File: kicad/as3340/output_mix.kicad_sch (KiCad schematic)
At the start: 28 parts, among them U1 TL074, U16 LM4040AIM3-2.5, U5 MAX333A, U6 AS3360, U8 DG442CY+

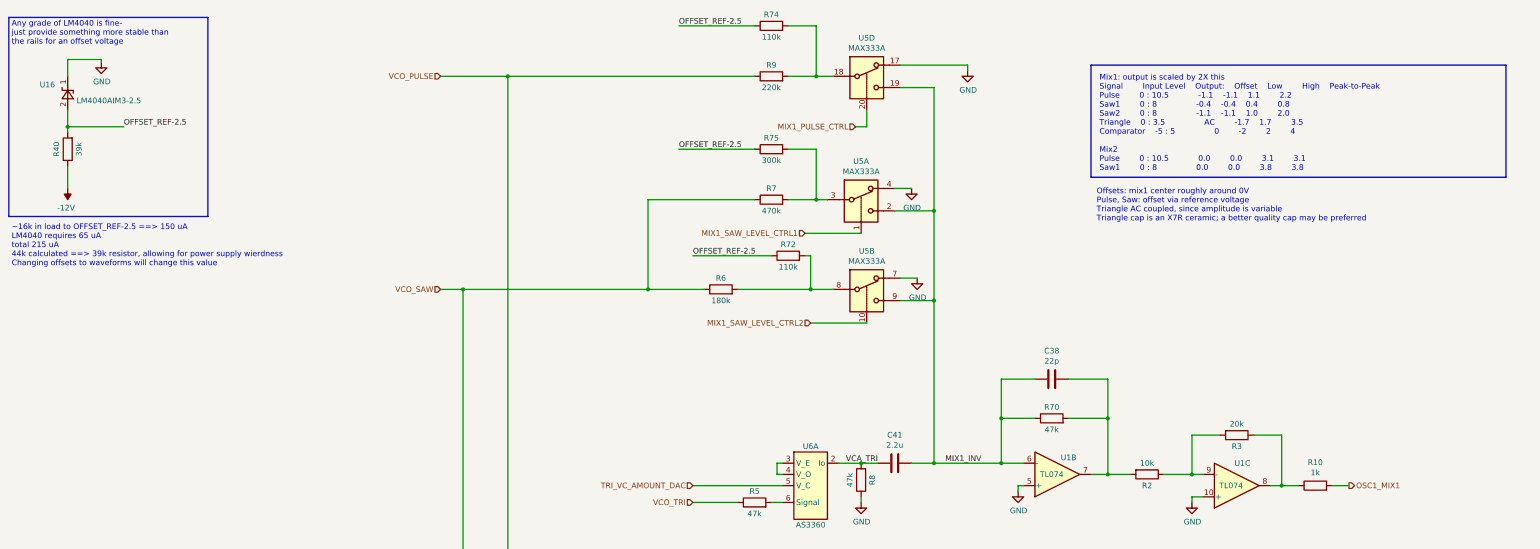
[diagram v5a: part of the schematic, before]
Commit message: working through 3340 changes.  Added sync circuits, DAC scaling changes, 16:1 multiplexor
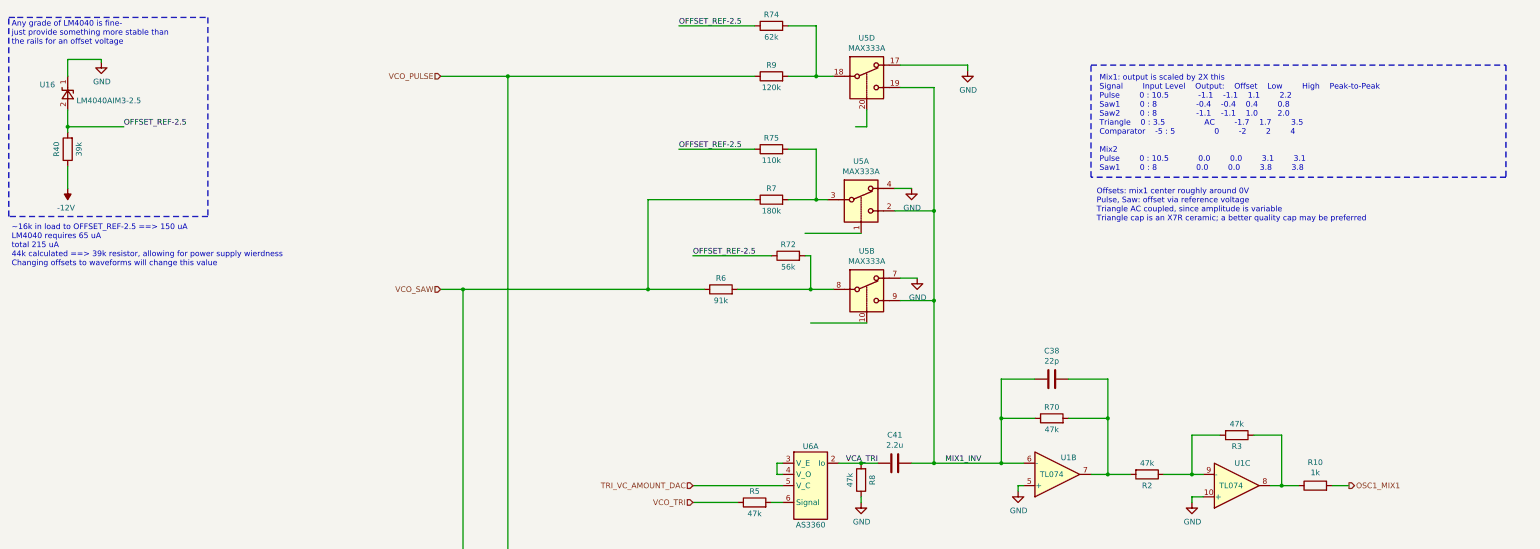
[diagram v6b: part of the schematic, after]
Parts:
- R2: value 10k -> 47k
- R3: value 20k -> 47k
- R6: value 180k -> 91k
- R7: value 470k -> 180k
- R72: value 110k -> 56k
- R74: value 110k -> 62k
- R75: value 300k -> 110k
- R9: value 220k -> 120k
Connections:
- net MIX1_PULSE_CTRL: no longer names the net of U5.20
- net MIX1_SAW_LEVEL_CTRL1: no longer names the net of U5.1
- net MIX1_SAW_LEVEL_CTRL2: no longer names the net of U5.10

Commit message: schematic capture z3340 about done; starting placement
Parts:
- removed R40: 39k, Resistor_SMD:R_0603_1608Metric, symbol Device:R
- removed R72: 56k, Resistor_SMD:R_0603_1608Metric, symbol Device:R
- removed R74: 62k, Resistor_SMD:R_0603_1608Metric, symbol Device:R
- removed R75: 110k, Resistor_SMD:R_0603_1608Metric, symbol Device:R
- removed U16: LM4040AIM3-2.5, Package_TO_SOT_SMD:SOT-23, symbol Reference_Voltage:LM4040DBZ-2.5
- removed U5: MAX333A, Package_SO:SOIC-20W_7.5x12.8mm_P1.27mm, symbol Analog_Switch:MAX333A
- removed U6: AS3360, Package_SO:SOIC-14_3.9x8.7mm_P1.27mm, symbol as3340:AS3360-Audio
- added C51: 2u2, Capacitor_THT:C_Rect_L7.2mm_W5.5mm_P5.00mm_FKS2_FKP2_MKS2_MKP2, symbol Device:C
- added R41: 150k, Resistor_SMD:R_0603_1608Metric, symbol Device:R
- added R43: 12k, Resistor_SMD:R_0603_1608Metric, symbol Device:R
- added U21: AS3364, Package_SO:SOIC-16_3.9x9.9mm_P1.27mm, symbol as3340:AS3364
- added U4: TL072, Package_SO:SSOP-8_3.9x5.05mm_P1.27mm, symbol Amplifier_Operational:TL072
- C41: value 2.2u -> 2u2; footprint Capacitor_SMD:C_1206_3216Metric -> Capacitor_THT:C_Rect_L7.2mm_W5.5mm_P5.00mm_FKS2_FKP2_MKS2_MKP2; LCSC Part C50254 -> (none)
- R7: value 180k -> 47k; LCSC Part (none) -> C25819
- U1: footprint Package_SO:SOIC-14_3.9x8.7mm_P1.27mm -> Package_SO:TSSOP-14_4.4x5mm_P0.65mm; LCSC Part C6963 -> C96507
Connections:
- net GND: now also R41.1, U4.5 (+); no longer R8.1
- net MIX2_PULSE_CTRL: now also U8.8; no longer U8.1
- net MIX2_SAW_CTRL: now also U8.9; no longer U8.16
- net VCO_PULSE: now also U8.7, R41.2; no longer U8.3
- net VCO_SAW: now also U8.11; no longer R7.1, U8.14
- net at R9.2: now also U21.7 (Iin)
- net at R13.1: now also U8.6; no longer U8.2
- net at R14.1: now also U8.10; no longer U8.15
- net at R2.1, R3.2, U1.9 (-): now also R43.2
- net at R6.2: now also U21.15 (Iin)
- net at R5.2: now also U21.10 (Iin)
- net at R7.2: now also U21.2 (Iin)
- net MIX1_INV: no longer names the net of C38.2, C41.1, R70.1, U1.6 (-)
- net MIX1_INV: now also C51.1, U21.5 (Iout)
- net VCA_TRI: no longer names the net of C41.2
- net VCA_TRI: now also U21.13 (Iout); no longer R8.2
- new net: C51.2, U21.12 (Iout)
- new net: R8.1, U21.4 (Iout), U4.6 (-)
- new net EXT_MODULATION: R7.1
- new net EXT_MOD_SCALED: R8.2, U4.7
- new net MOD_VCA_AMOUNT_DAC: U21.3 (Vc)
- new net PULSE_VCA_AMOUNT_DAC: R43.1, U21.6 (Vc)
- new net SAW_VCA_AMOUNT_DAC: U21.14 (Vc)
- new net TRI_VCA_AMOUNT_DAC: U21.11 (Vc)
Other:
- note added: "External Modulation Scaling"
- note added: "Impedance from DAC ~12k"
- note added: "Outpus One and Two Scaling: One has VCA controlled output levels that are AC coupled (tri / saw) or at least offset (pulse). No AC coupling on the pulse to keep it looking sharp for modulation. Output Two fixed levels between Pulse and Saw and unipolar."
- note removed: "Any grade of LM4040 is fine- just provide something more stable than the rails for an offset voltage"
- note removed: "~16k in load to OFFSET_REF-2.5 ==> 150 uA LM4040 requires 65 uA total 215 uA 44k calculated ==> 39k resistor, allowing for power supply wierdness Changing offsets to waveforms will change this value"
- moved on the sheet: C38, C40, R10, R11, R13, R14, R2, R3, R5, R6, R65, R66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

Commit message: z3340 placement getting close to good
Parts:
- R10, R65: value 1k -> 51; LCSC Part C21190 -> (none)
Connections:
- net GND: now also U1.12 (+), U1.5 (+); no longer U1.12 (+), U1.5 (+)
- net MIX2_PULSE_CTRL: now also U8.1; no longer U8.8
- net MIX2_SAW_CTRL: now also U8.16; no longer U8.9
- net VCO_PULSE: now also U8.3; no longer U8.7
- net VCO_SAW: now also U8.14; no longer U8.11
- net at R13.1: now also U8.2; no longer U8.6
- net at R14.1: now also U8.15; no longer U8.10
- net at C38.2, C41.1, C51.1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: now also U1.13 (-); no longer U1.6 (-)
- net at C38.1, R2.2, R70.2: now also U1.14; no longer U1.7
- net at R65.1, R73.1: now also U1.7; no longer U1.14
- net at R71.1, R73.2: now also U1.6 (-); no longer U1.13 (-)
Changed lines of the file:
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@@
     (stroke (width 0) (type default))
   )
-  (wire (pts (xy 78.74 54.61) (xy 93.98 54.61))
+  (wire (pts (xy 80.01 54.61) (xy 93.98 54.61))
     (stroke (width 0) (type default))
   )
@@
     (stroke (width 0) (type default))
   )
-  (wire (pts (xy 102.87 144.78) (xy 83.82 144.78))
+  (wire (pts (xy 102.87 146.05) (xy 86.36 146.05))
     (stroke (width 0) (type default))
   )
@@
     (stroke (width 0) (type default))
   )
-  (wire (pts (xy 102.87 147.32) (xy 102.87 144.78))
+  (wire (pts (xy 102.87 146.05) (xy 102.87 147.32))
     (stroke (width 0) (type default))
   )
@@
     (effects (font (size 1.27 1.27)) (justify left))
   )
-  (hierarchical_label "PULSE_VCA_AMOUNT_DAC" (shape input) (at 78.74 54.61 180) (fields_autoplaced)
+  (hierarchical_label "PULSE_VCA_AMOUNT_DAC" (shape input) (at 80.01 54.61 180) (fields_autoplaced)
     (effects (font (size 1.27 1.27)) (justify right))
   )
@@
     (effects (font (size 1.27 1.27)) (justify right))
   )
-  (hierarchical_label "MIX2_SAW_CTRL" (shape input) (at 83.82 144.78 180) (fields_autoplaced)
+  (hierarchical_label "MIX2_SAW_CTRL" (shape input) (at 86.36 146.05 180) (fields_autoplaced)
     (effects (font (size 1.27 1.27)) (justify right))
   )
@@
     )
   )
-  (symbol (lib_id "Analog_Switch:DG441xJ") (at 102.87 133.35 180) (unit 2)
+  (symbol (lib_id "Analog_Switch:DG441xJ") (at 102.87 133.35 180) (unit 1)
     (in_bom yes) (on_board yes) (dnp no)
     (property "Reference" "U8" (at 102.87 137.795 0)
@@
       (project "as3340"
         (path "/7079bdb0-a00e-4bac-b257-cbcf2c91bbd6/00000000-0000-0000-0000-00006269dd41"
-          (reference "U8") (unit 2)
-        )
-      )
-    )
-  )
-  (symbol (lib_id "Analog_Switch:DG441xJ") (at 102.87 152.4 180) (unit 3)
+          (reference "U8") (unit 1)
+        )
+      )
+    )
+  )
+  (symbol (lib_id "Analog_Switch:DG441xJ") (at 102.87 152.4 180) (unit 4)
     (in_bom yes) (on_board yes) (dnp no)
     (property "Reference" "U8" (at 102.87 156.845 0)
@@
       (project "as3340"
         (path "/7079bdb0-a00e-4bac-b257-cbcf2c91bbd6/00000000-0000-0000-0000-00006269dd41"
-          (reference "U8") (unit 3)
-        )
-      )
-    )
-  )
-  (symbol (lib_id "Amplifier_Operational:TL074") (at 151.13 88.9 0) (mirror x) (unit 2)
+          (reference "U8") (unit 4)
+        )
+      )
+    )
+  )
+  (symbol (lib_id "Amplifier_Operational:TL074") (at 151.13 88.9 0) (mirror x) (unit 4)
     (in_bom yes) (on_board yes) (dnp no)
     (property "Reference" "U1" (at 153.67 85.09 0)
@@
       (project "as3340"
         (path "/7079bdb0-a00e-4bac-b257-cbcf2c91bbd6/00000000-0000-0000-0000-00006269dd41"
-          (reference "U1") (unit 2)
+          (reference "U1") (unit 4)
         )
       )
@@
       (effects (font (size 1.27 1.27)))
     )
-    (property "Value" "1k" (at 210.82 135.4836 90)
+    (property "Value" "51" (at 210.82 135.4836 90)
       (effects (font (size 1.27 1.27)))
     )
@@
       (effects (font (size 1.27 1.27)) hide)
     )
-    (property "LCSC Part" "C21190" (at 210.82 138.43 0)
+    (property "LCSC Part" "" (at 210.82 138.43 0)
       (effects (font (size 1.27 1.27)) hide)
     )
@@
       (effects (font (size 1.27 1.27)))
     )
-    (property "Value" "1k" (at 209.55 88.4936 90)
+    (property "Value" "51" (at 209.55 88.4936 90)
       (effects (font (size 1.27 1.27)))
     )
@@
       (effects (font (size 1.27 1.27)) hide)
     )
-    (property "LCSC Part" "C21190" (at 209.55 91.44 0)
+    (property "LCSC Part" "" (at 209.55 91.44 0)
       (effects (font (size 1.27 1.27)) hide)
     )
@@
     )
   )
-  (symbol (lib_id "Amplifier_Operational:TL074") (at 193.04 138.43 0) (mirror x) (unit 4)
+  (symbol (lib_id "Amplifier_Operational:TL074") (at 193.04 138.43 0) (mirror x) (unit 2)
     (in_bom yes) (on_board yes) (dnp no)
     (property "Reference" "U1" (at 194.31 133.35 0)
@@
       (project "as3340"
         (path "/7079bdb0-a00e-4bac-b257-cbcf2c91bbd6/00000000-0000-0000-0000-00006269dd41"
-          (reference "U1") (unit 4)
-        )
-      )
+          (reference "U1") (unit 2)
+        )
+      )
